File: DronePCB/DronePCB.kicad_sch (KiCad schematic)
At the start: 1 part, among them U1 RASPBERRY_PI_ZERO_2_W

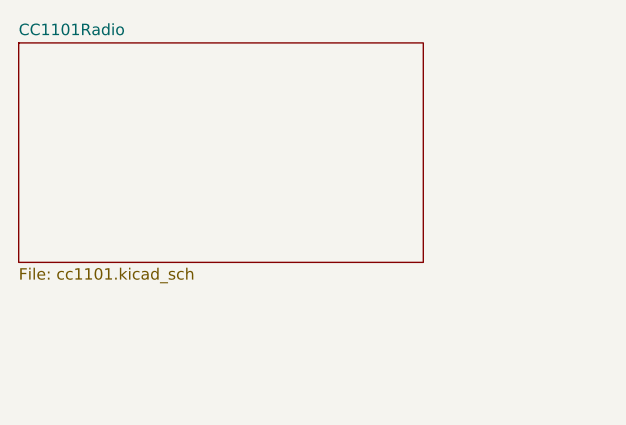
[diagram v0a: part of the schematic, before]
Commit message: Completed CC1101 Radio Schematic
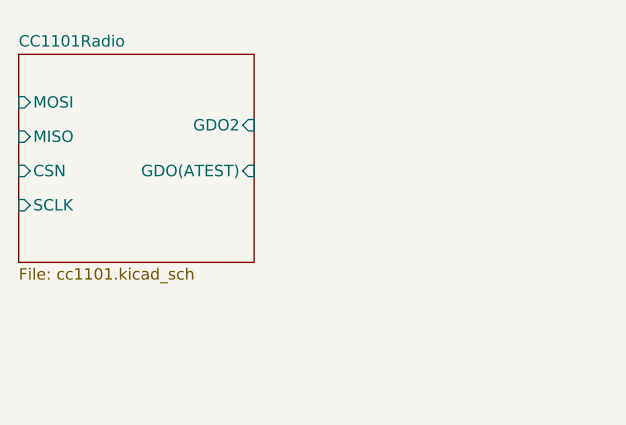
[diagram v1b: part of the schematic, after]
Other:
- sheet CC1101Radio ports: added CSN, GDO(ATEST), GDO2, MISO, MOSI, SCLK; removed none
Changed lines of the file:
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@@
 	)
 	(sheet
-		(at 52.578 79.756)
-		(size 44.958 24.384)
+		(at 52.578 81.026)
+		(size 26.162 23.114)
 		(exclude_from_sim no)
 		(in_bom yes)
@@
 		)
 		(property "Sheetname" "CC1101Radio"
-			(at 52.578 79.0444 0)
+			(at 52.578 80.3144 0)
 			(effects
 				(font
@@
 			)
 		)
+		(pin "GDO2" input
+			(at 78.74 88.9 0)
+			(effects
+				(font
+					(size 1.27 1.27)
+				)
+				(justify right)
+			)
+		)
+		(pin "MOSI" input
+			(at 52.578 86.36 180)
+			(effects
+				(font
+					(size 1.27 1.27)
+				)
+				(justify left)
+			)
+		)
+		(pin "MISO" input
+			(at 52.578 90.17 180)
+			(effects
+				(font
+					(size 1.27 1.27)
+				)
+				(justify left)
+			)
+		)
+		(pin "GDO(ATEST)" input
+			(at 78.74 93.98 0)
+			(effects
+				(font
+					(size 1.27 1.27)
+				)
+				(justify right)
+			)
+		)
+		(pin "CSN" input
+			(at 52.578 93.98 180)
+			(effects
+				(font
+					(size 1.27 1.27)
+				)
+				(justify left)
+			)
+		)
+		(pin "SCLK" input
+			(at 52.578 97.79 180)
+			(effects
+				(font
+					(size 1.27 1.27)
+				)
+				(justify left)
+			)
+		)

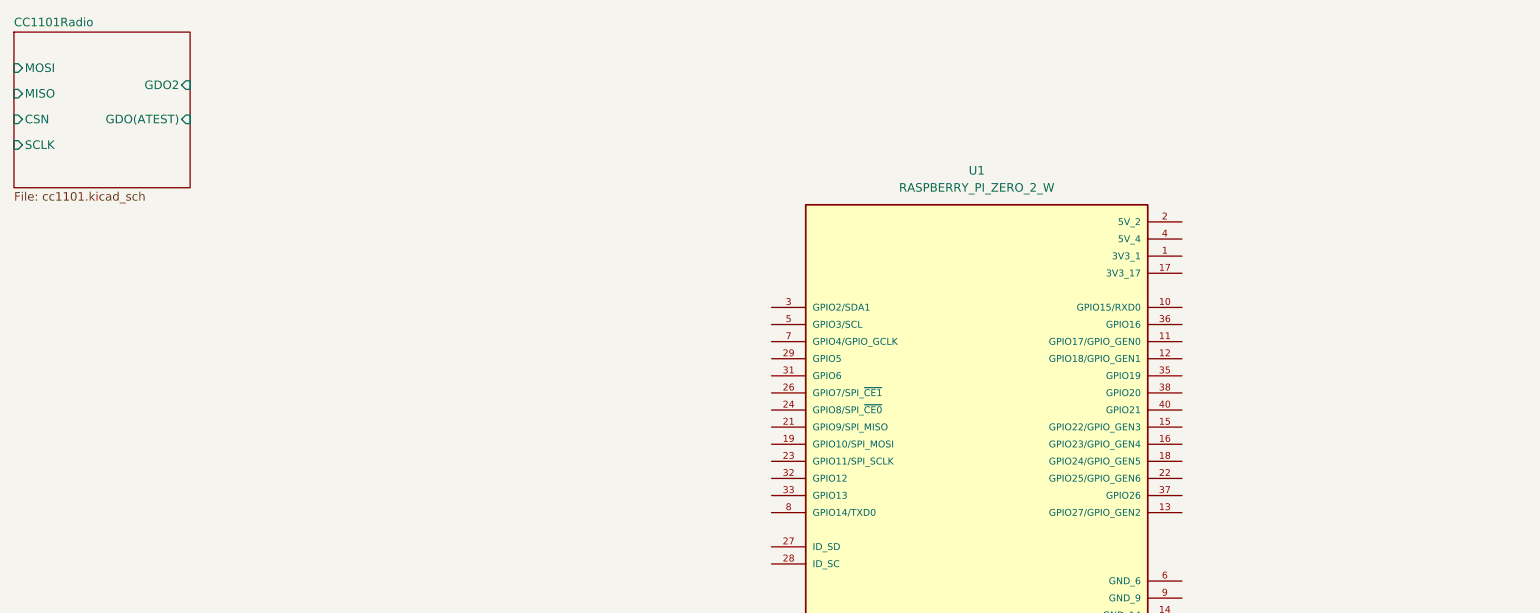
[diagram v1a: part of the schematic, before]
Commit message: Finished and wired up CC1101 and Microphone circuits
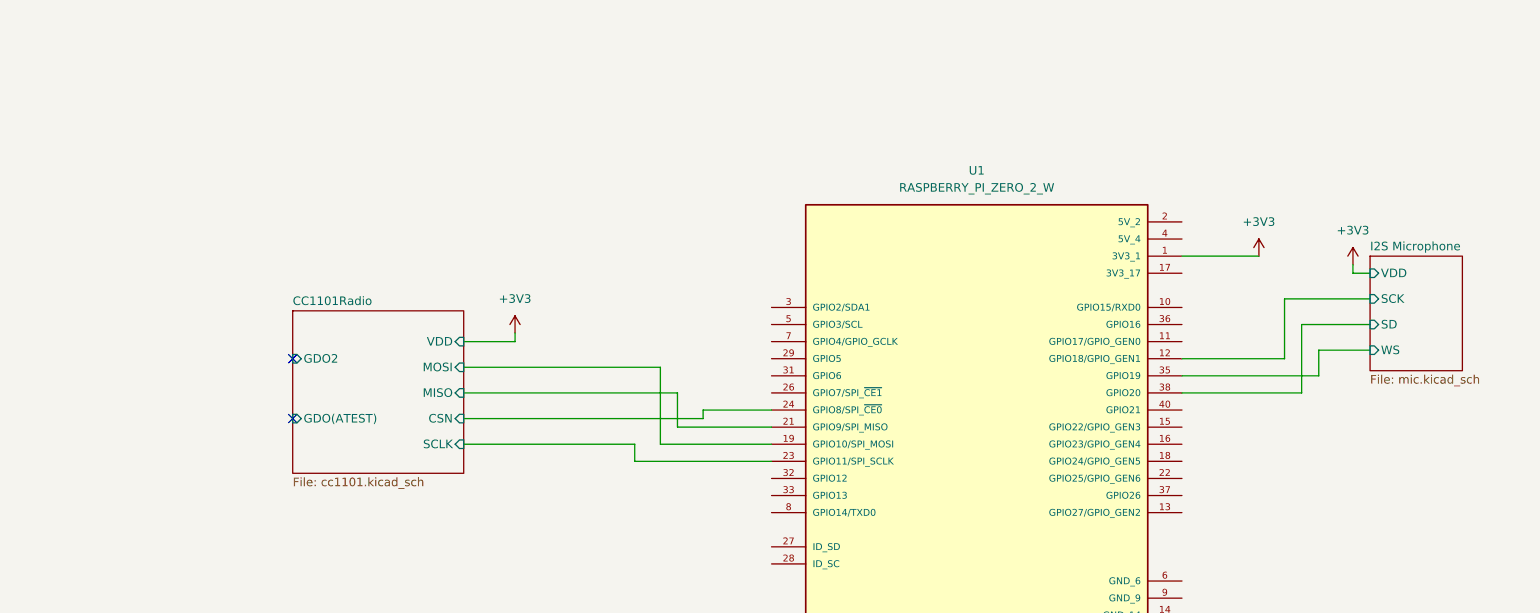
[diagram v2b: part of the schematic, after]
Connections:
- net CC1101Radio/CSN: now also U1.24 (GPIO8/SPI_~{CE0})
- net CC1101Radio/MISO: now also U1.21 (GPIO9/SPI_MISO)
- net CC1101Radio/MOSI: now also U1.19 (GPIO10/SPI_MOSI)
- net CC1101Radio/SCLK: now also U1.23 (GPIO11/SPI_SCLK)
- net +3V3: now reaches U1.1 (3V3_1)
- net I2S Microphone/SCK: now reaches U1.12 (GPIO18/GPIO_GEN1)
- net I2S Microphone/WS: now reaches U1.35 (GPIO19)
- net I2S Microphone/SD: now reaches U1.38 (GPIO20)
- no-connect marks 0 -> 2
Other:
- added sheet I2S Microphone (mic.kicad_sch)
- sheet CC1101Radio ports: added VDD; removed none

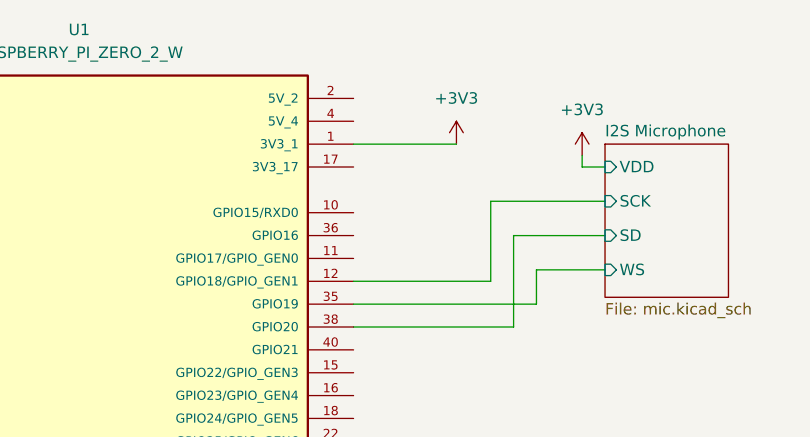
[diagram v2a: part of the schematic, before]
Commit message: Added mic schematic, extra DNP decouple Cap, fixed 3v3 wiring
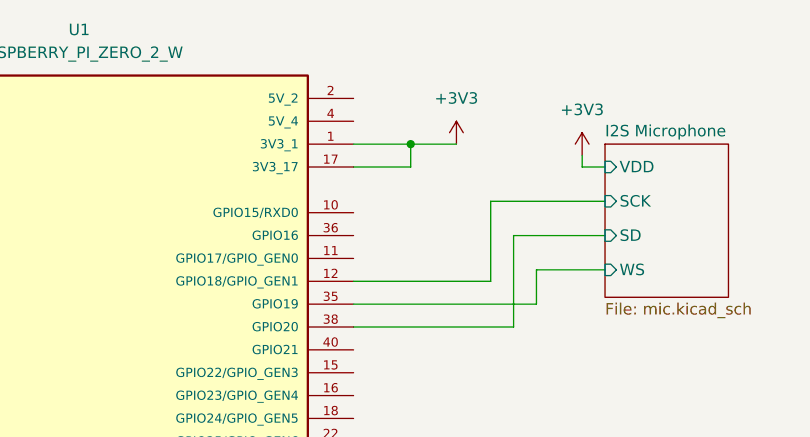
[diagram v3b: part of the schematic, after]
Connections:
- net +3V3: now also U1.17 (3V3_17)
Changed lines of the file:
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@@
 		(company "Penn State EE")
+	)
+	(junction
+		(at 232.41 114.3)
+		(diameter 0)
+		(color 0 0 0 0)
 	)
 	(no_connect
@@
 	(wire
 		(pts
+			(xy 226.06 116.84) (xy 232.41 116.84)
+		)
+		(stroke
+			(width 0)
+			(type default)
+		)
+	)
+	(wire
+		(pts
 			(xy 226.06 129.54) (xy 241.3 129.54)
 		)
@@
 	(wire
 		(pts
+			(xy 232.41 116.84) (xy 232.41 114.3)
+		)
+		(stroke
+			(width 0)
+			(type default)
+		)
+	)
+	(wire
+		(pts
 			(xy 254 116.84) (xy 251.46 116.84)
 		)
@@
 	(wire
 		(pts
-			(xy 237.49 114.3) (xy 226.06 114.3)
+			(xy 237.49 114.3) (xy 232.41 114.3)
 		)
 		(stroke
@@
 		)
 		(stroke
+			(width 0)
+			(type default)
+		)
+	)
+	(wire
+		(pts
+			(xy 232.41 114.3) (xy 226.06 114.3)
+		)
+		(stroke

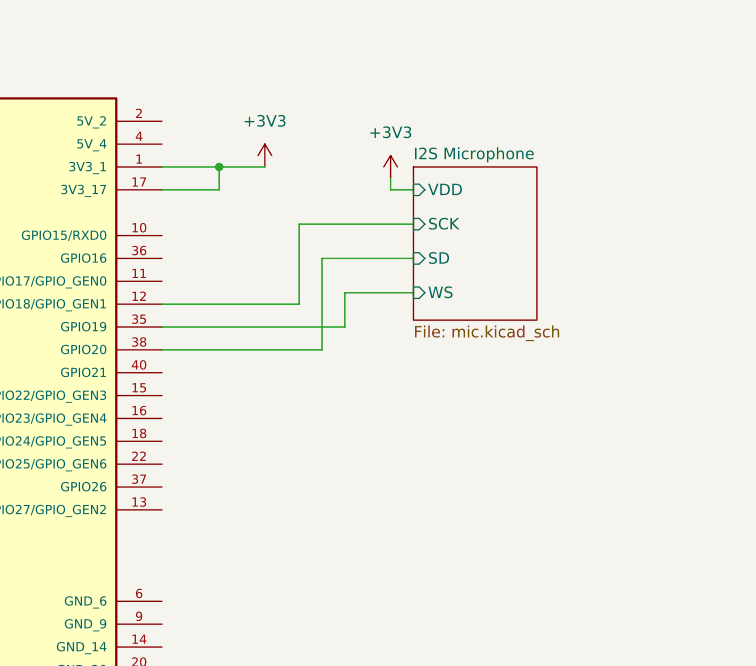
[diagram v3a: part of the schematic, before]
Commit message: Incorperated IR Ciruit into main schematic
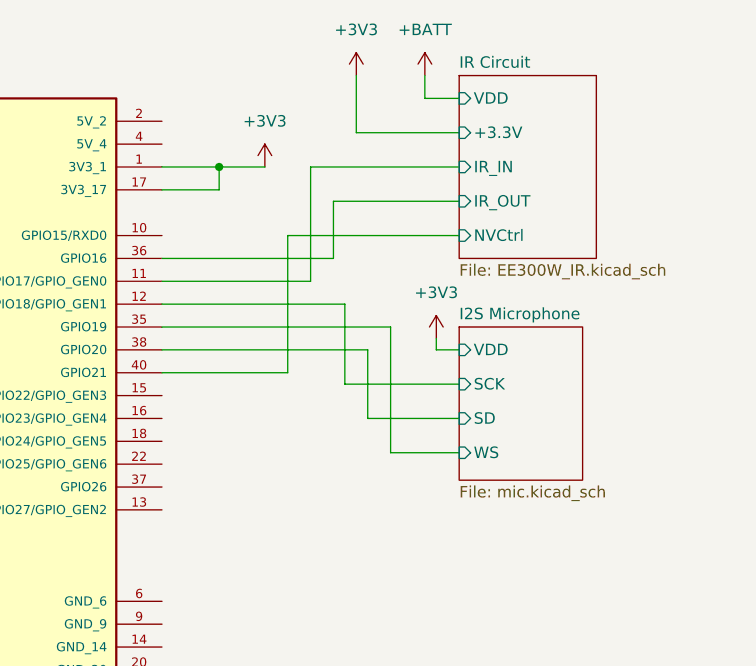
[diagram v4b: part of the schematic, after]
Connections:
- net IR Circuit/IR_IN: now reaches U1.11 (GPIO17/GPIO_GEN0)
- net IR Circuit/IR_OUT: now reaches U1.36 (GPIO16)
- net IR Circuit/NVCtrl: now reaches U1.40 (GPIO21)
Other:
- added sheet IR Circuit (EE300W_IR.kicad_sch)

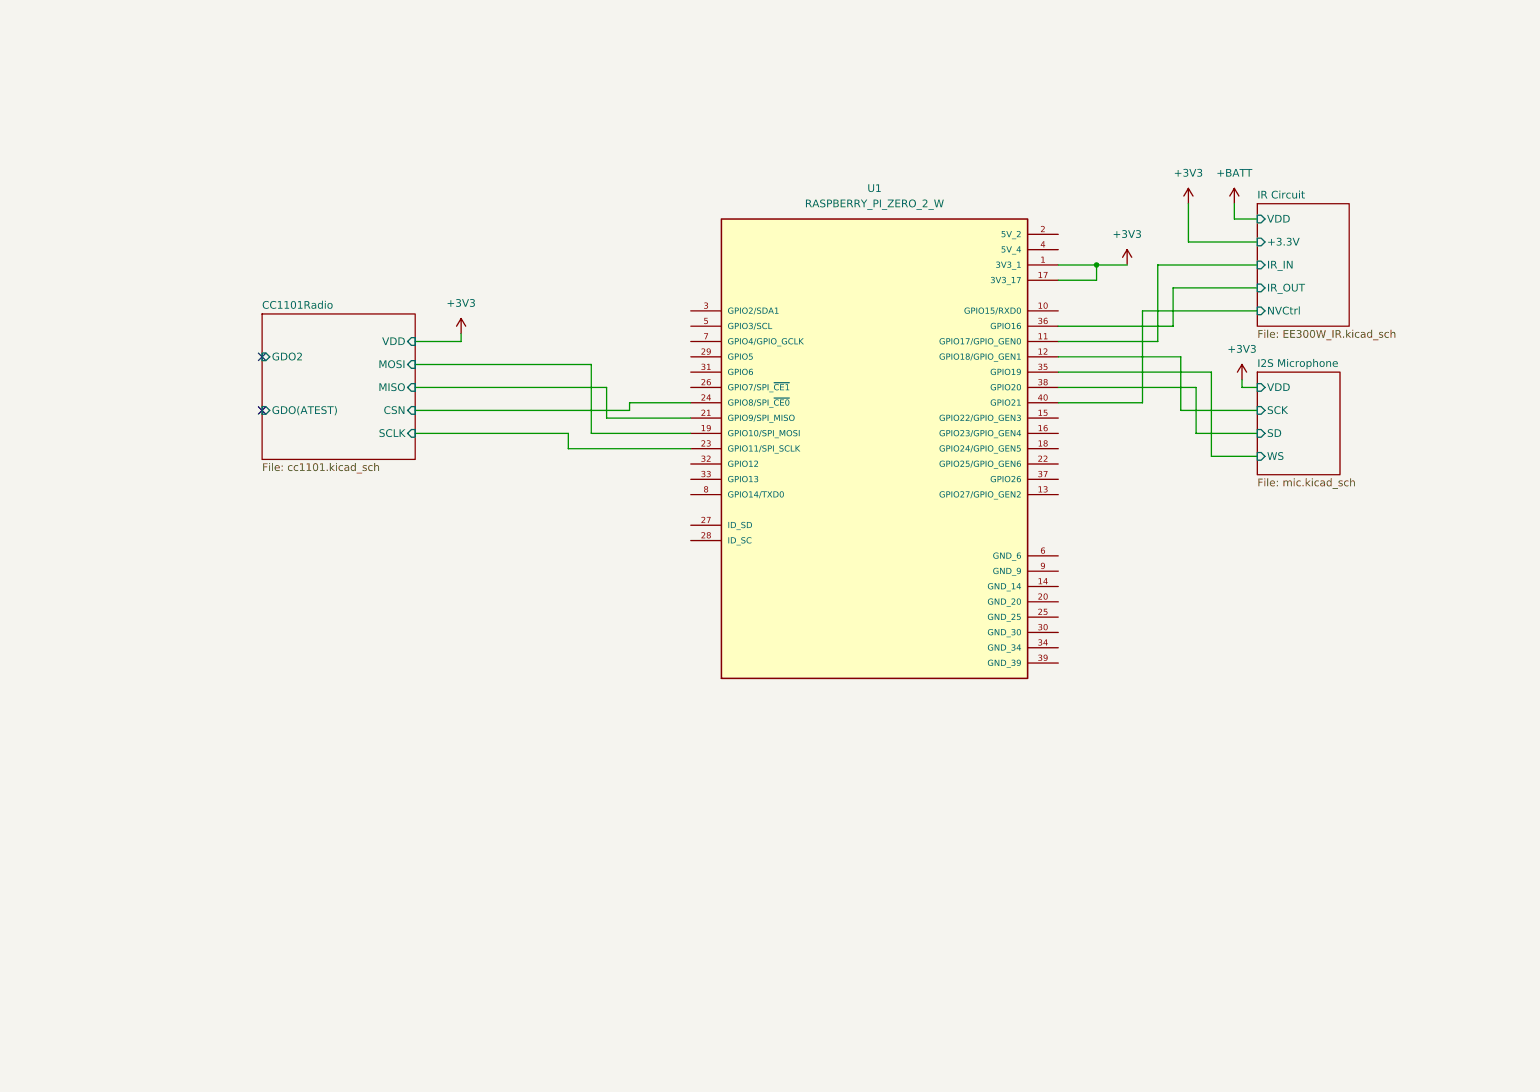
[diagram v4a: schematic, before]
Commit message: added motor driver
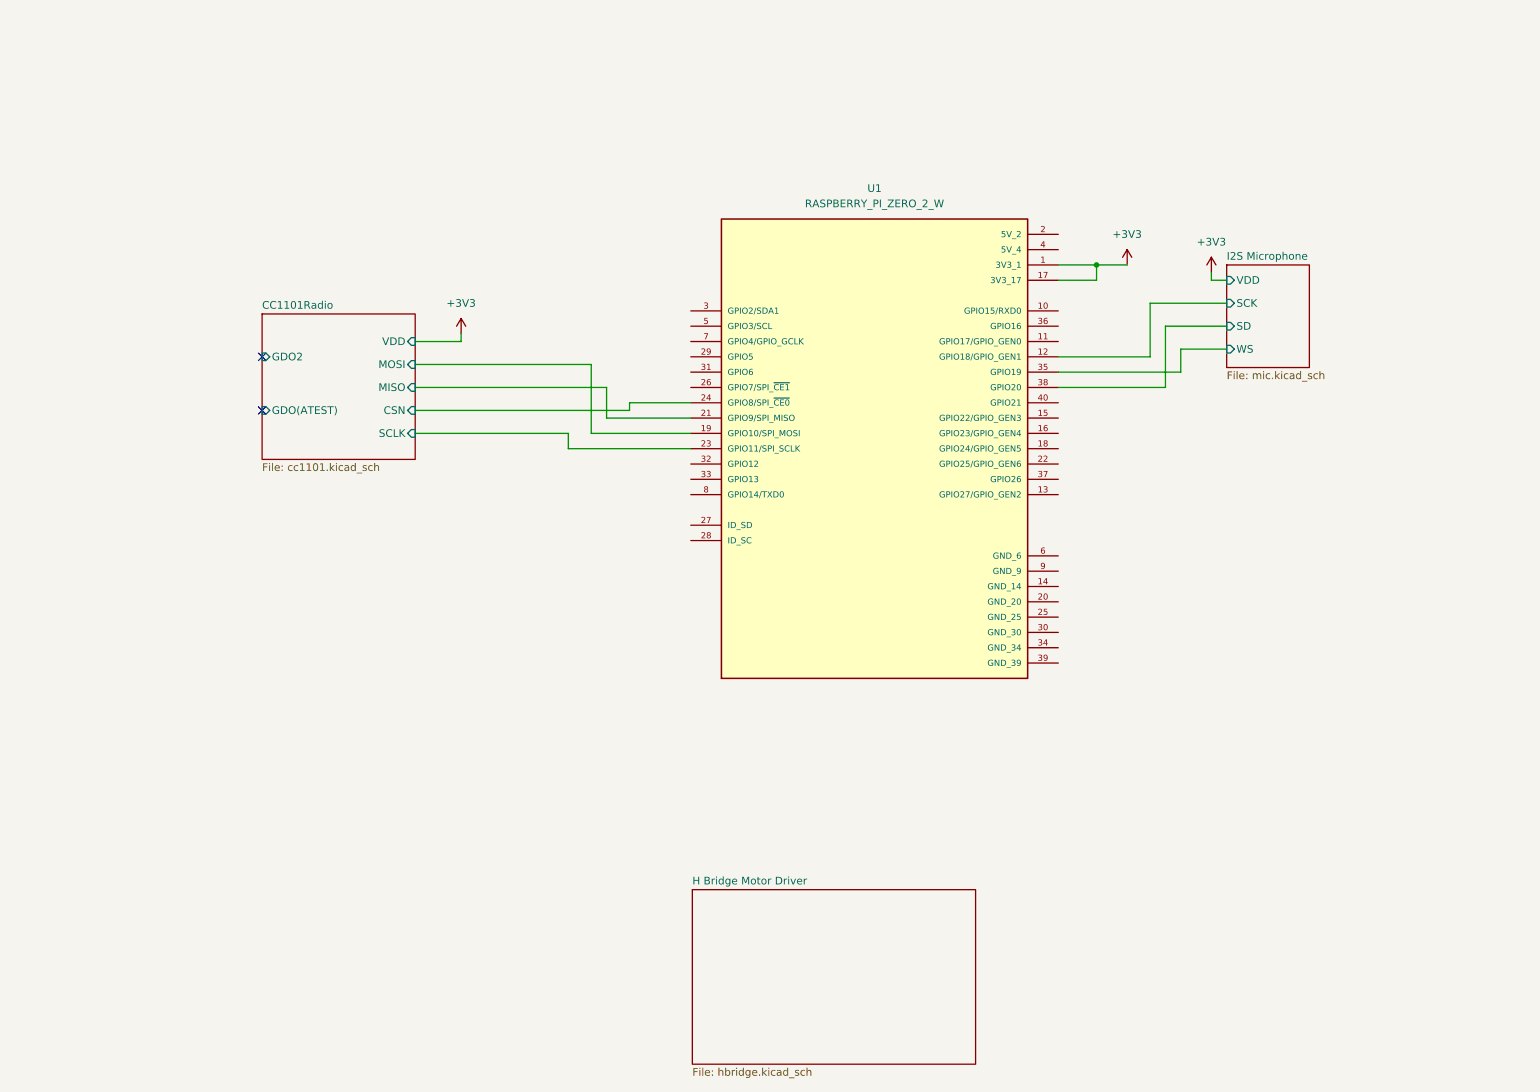
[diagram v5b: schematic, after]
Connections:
- net IR Circuit/IR_IN: no longer names the net of U1.11 (GPIO17/GPIO_GEN0)
- net IR Circuit/IR_OUT: no longer names the net of U1.36 (GPIO16)
- net IR Circuit/NVCtrl: no longer names the net of U1.40 (GPIO21)
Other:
- removed sheet IR Circuit
- added sheet H Bridge Motor Driver (hbridge.kicad_sch)

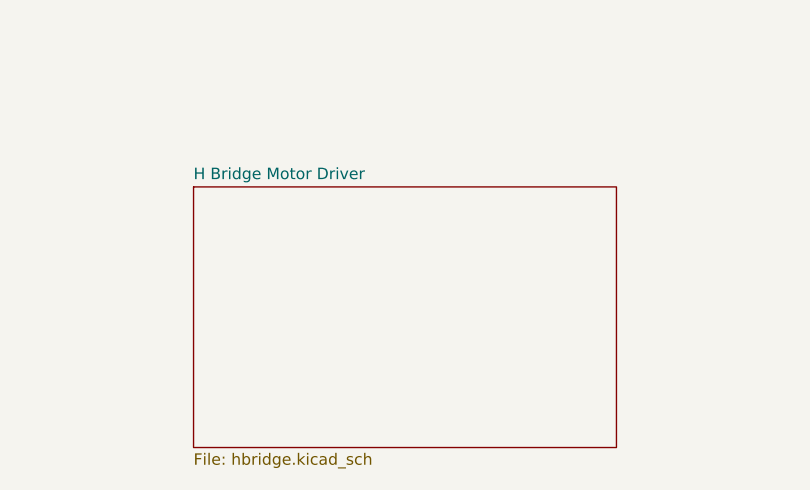
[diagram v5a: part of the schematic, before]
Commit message: Fixed a connection in battery circuit and updated project to KiCAD 10.0.0
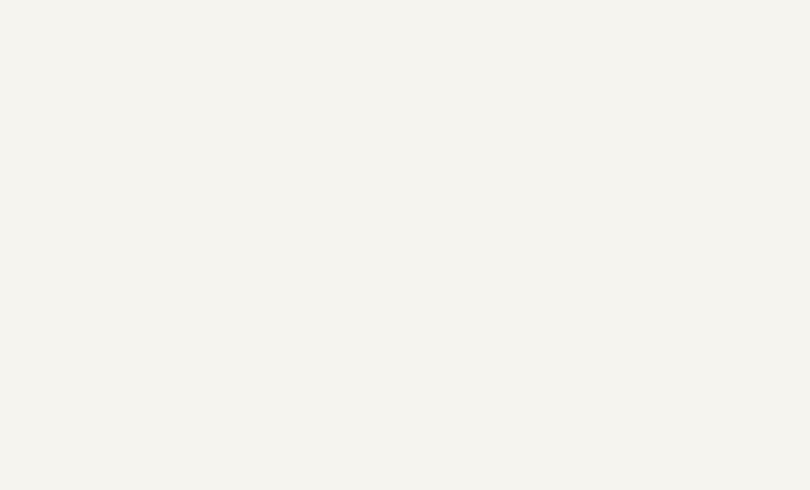
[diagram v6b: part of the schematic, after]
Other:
- removed sheet H Bridge Motor Driver
